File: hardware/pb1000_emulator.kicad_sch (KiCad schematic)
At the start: 1 part, among them U1 Raspberry Pi Pico 2 (RP2350)

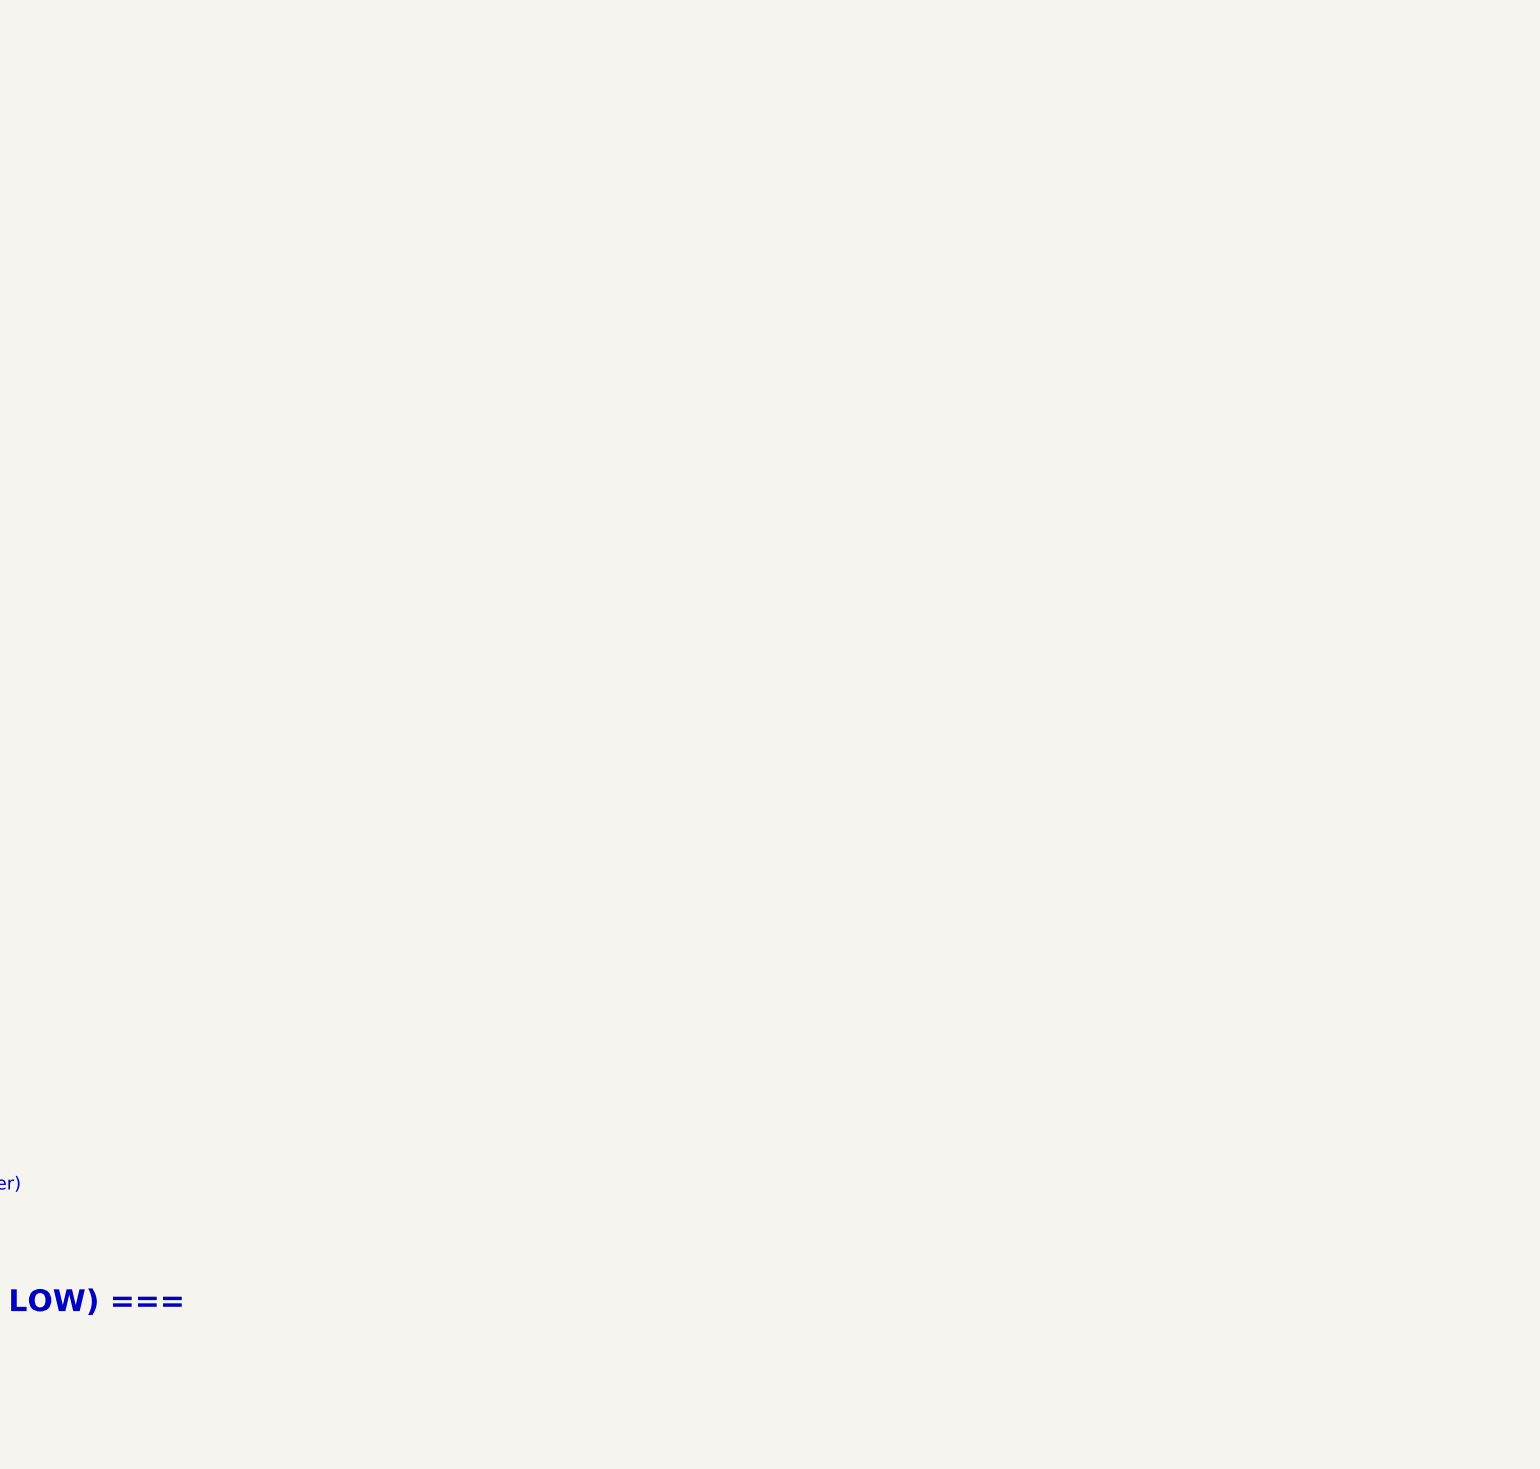
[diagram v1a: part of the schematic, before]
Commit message: VFDDがデバッグ動作のままで性能が低下していたのを修正、FDイメージ操作ツールでPCからのファイル転送時に必ずファイル名を大文字にするよう修正(Claude Code)
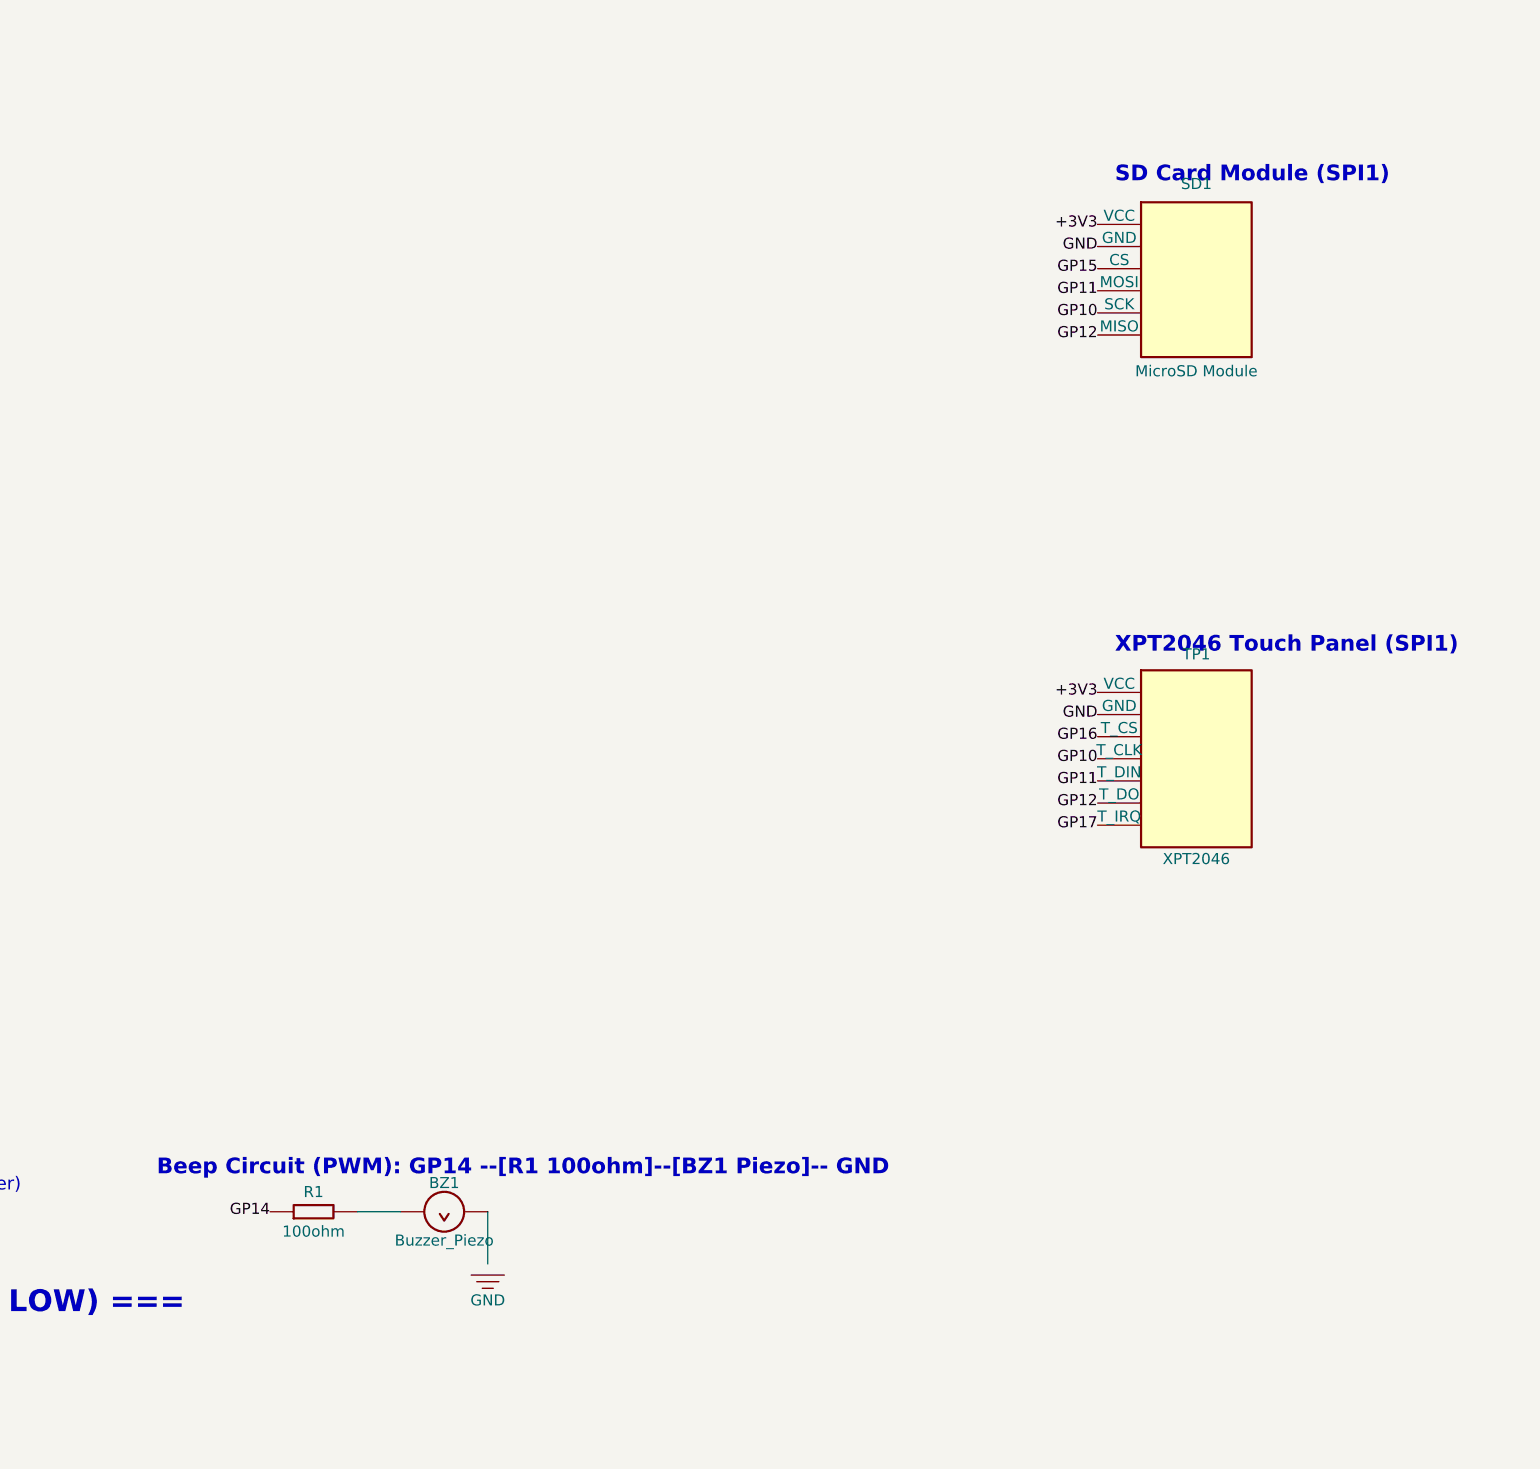
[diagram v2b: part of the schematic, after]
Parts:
- added BZ1: Buzzer_Piezo, symbol Local:Buzzer_Piezo
- added R1: 100ohm, symbol Local:R
- added SD1: MicroSD Module, symbol Local:SD_Card
- added TP1: XPT2046, symbol Local:XPT2046
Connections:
- new net: BZ1.1 (+), R1.2
- new net +3V3: SD1.1 (VCC), TP1.1 (VCC)
- new net GND: BZ1.2 (K), SD1.2 (GND), TP1.2 (GND)
- new net GP10: SD1.5 (SCK), TP1.4 (T_CLK)
- new net GP11: SD1.4 (MOSI), TP1.5 (T_DIN)
- new net GP12: SD1.6 (MISO), TP1.6 (T_DO)
- new net GP14: R1.1
- new net GP15: SD1.3 (CS)
- new net GP16: TP1.3 (T_CS)
- new net GP17: TP1.7 (T_IRQ)
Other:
- note added: "Beep Circuit (PWM): GP14 --[R1 100ohm]--[BZ1 Piezo]-- GND"
- note added: "SD Card Module (SPI1)"
- note added: "XPT2046 Touch Panel (SPI1)"
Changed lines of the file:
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@@
     (effects (font (size 1.5 1.5)) (justify left))
   )
+  (text "Beep Circuit (PWM): GP14 --[R1 100ohm]--[BZ1 Piezo]-- GND" (at 232 202 0)
+    (effects (font (size 1.8 1.8) (bold yes)) (justify left))
+  )
+  (label "GP14" (at 245 207 180)
+    (effects (font (size 1.27 1.27)) (justify right))
+  )
+  (symbol (lib_id "Local:R") (at 250 207 0) (unit 1)
+    (in_bom yes) (on_board yes) (fields_autoplaced)
+    (property "Reference" "R1" (id 0) (at 250 204.73 0)
+      (effects (font (size 1.27 1.27)))
+    )
+    (property "Value" "100ohm" (id 1) (at 250 209.27 0)
+      (effects (font (size 1.27 1.27)))
+    )
+  )
+  (wire (pts (xy 255 207) (xy 260 207))
+    (stroke (width 0) (type default))
+  )
+  (symbol (lib_id "Local:Buzzer_Piezo") (at 265 207 0) (unit 1)
+    (in_bom yes) (on_board yes) (fields_autoplaced)
+    (property "Reference" "BZ1" (id 0) (at 265 203.698 0)
+      (effects (font (size 1.27 1.27)))
+    )
+    (property "Value" "Buzzer_Piezo" (id 1) (at 265 210.302 0)
+      (effects (font (size 1.27 1.27)))
+    )
+  )
+  (wire (pts (xy 270 207) (xy 270 213))
+    (stroke (width 0) (type default))
+  )
+  (symbol (lib_id "power:GND") (at 270 213 0) (unit 1)
+    (in_bom yes) (on_board yes) (fields_autoplaced)
+    (property "Reference" "#PWR01" (id 0) (at 270 213 0)
+      (effects (font (size 1.27 1.27)) hide)
+    )
+    (property "Value" "GND" (id 1) (at 270 217.17 0)
+      (effects (font (size 1.27 1.27)))
+    )
+  )
+  (text "SD Card Module (SPI1)" (at 342 88 0)
+    (effects (font (size 1.8 1.8) (bold yes)) (justify left))
+  )
+  (symbol (lib_id "Local:SD_Card") (at 345 100 0) (unit 1)
+    (in_bom yes) (on_board yes) (fields_autoplaced)
+    (property "Reference" "SD1" (id 0) (at 351.35 89 0)
+      (effects (font (size 1.27 1.27)))
+    )
+    (property "Value" "MicroSD Module" (id 1) (at 351.35 110.5 0)
+      (effects (font (size 1.27 1.27)))
+    )
+  )
+  (label "+3V3" (at 340 93.65 180)
+    (effects (font (size 1.27 1.27)) (justify right))
+  )
+  (label "GND" (at 340 96.19 180)
+    (effects (font (size 1.27 1.27)) (justify right))
+  )
+  (label "GP15" (at 340 98.73 180)
+    (effects (font (size 1.27 1.27)) (justify right))
+  )
+  (label "GP11" (at 340 101.27 180)
+    (effects (font (size 1.27 1.27)) (justify right))
+  )
+  (label "GP10" (at 340 103.81 180)
+    (effects (font (size 1.27 1.27)) (justify right))
+  )
+  (label "GP12" (at 340 106.35 180)
+    (effects (font (size 1.27 1.27)) (justify right))
+  )
+  (text "XPT2046 Touch Panel (SPI1)" (at 342 142 0)
+    (effects (font (size 1.8 1.8) (bold yes)) (justify left))
+  )
+  (symbol (lib_id "Local:XPT2046") (at 345 155 0) (unit 1)
+    (in_bom yes) (on_board yes) (fields_autoplaced)
+    (property "Reference" "TP1" (id 0) (at 351.35 143 0)
+      (effects (font (size 1.27 1.27)))
+    )
+    (property "Value" "XPT2046" (id 1) (at 351.35 166.5 0)
+      (effects (font (size 1.27 1.27)))
+    )
+  )
+  (label "+3V3" (at 340 147.38 180)
+    (effects (font (size 1.27 1.27)) (justify right))
+  )
+  (label "GND" (at 340 149.92 180)
+    (effects (font (size 1.27 1.27)) (justify right))
+  )
+  (label "GP16" (at 340 152.46 180)
+    (effects (font (size 1.27 1.27)) (justify right))
+  )
+  (label "GP10" (at 340 155 180)
+    (effects (font (size 1.27 1.27)) (justify right))
+  )
+  (label "GP11" (at 340 157.54 180)
+    (effects (font (size 1.27 1.27)) (justify right))
+  )
+  (label "GP12" (at 340 160.08 180)
+    (effects (font (size 1.27 1.27)) (justify right))
+  )
+  (label "GP17" (at 340 162.62 180)
+    (effects (font (size 1.27 1.27)) (justify right))
+  )
 )

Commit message: タイマー機能の実装ほぼ完了(Claude Code)
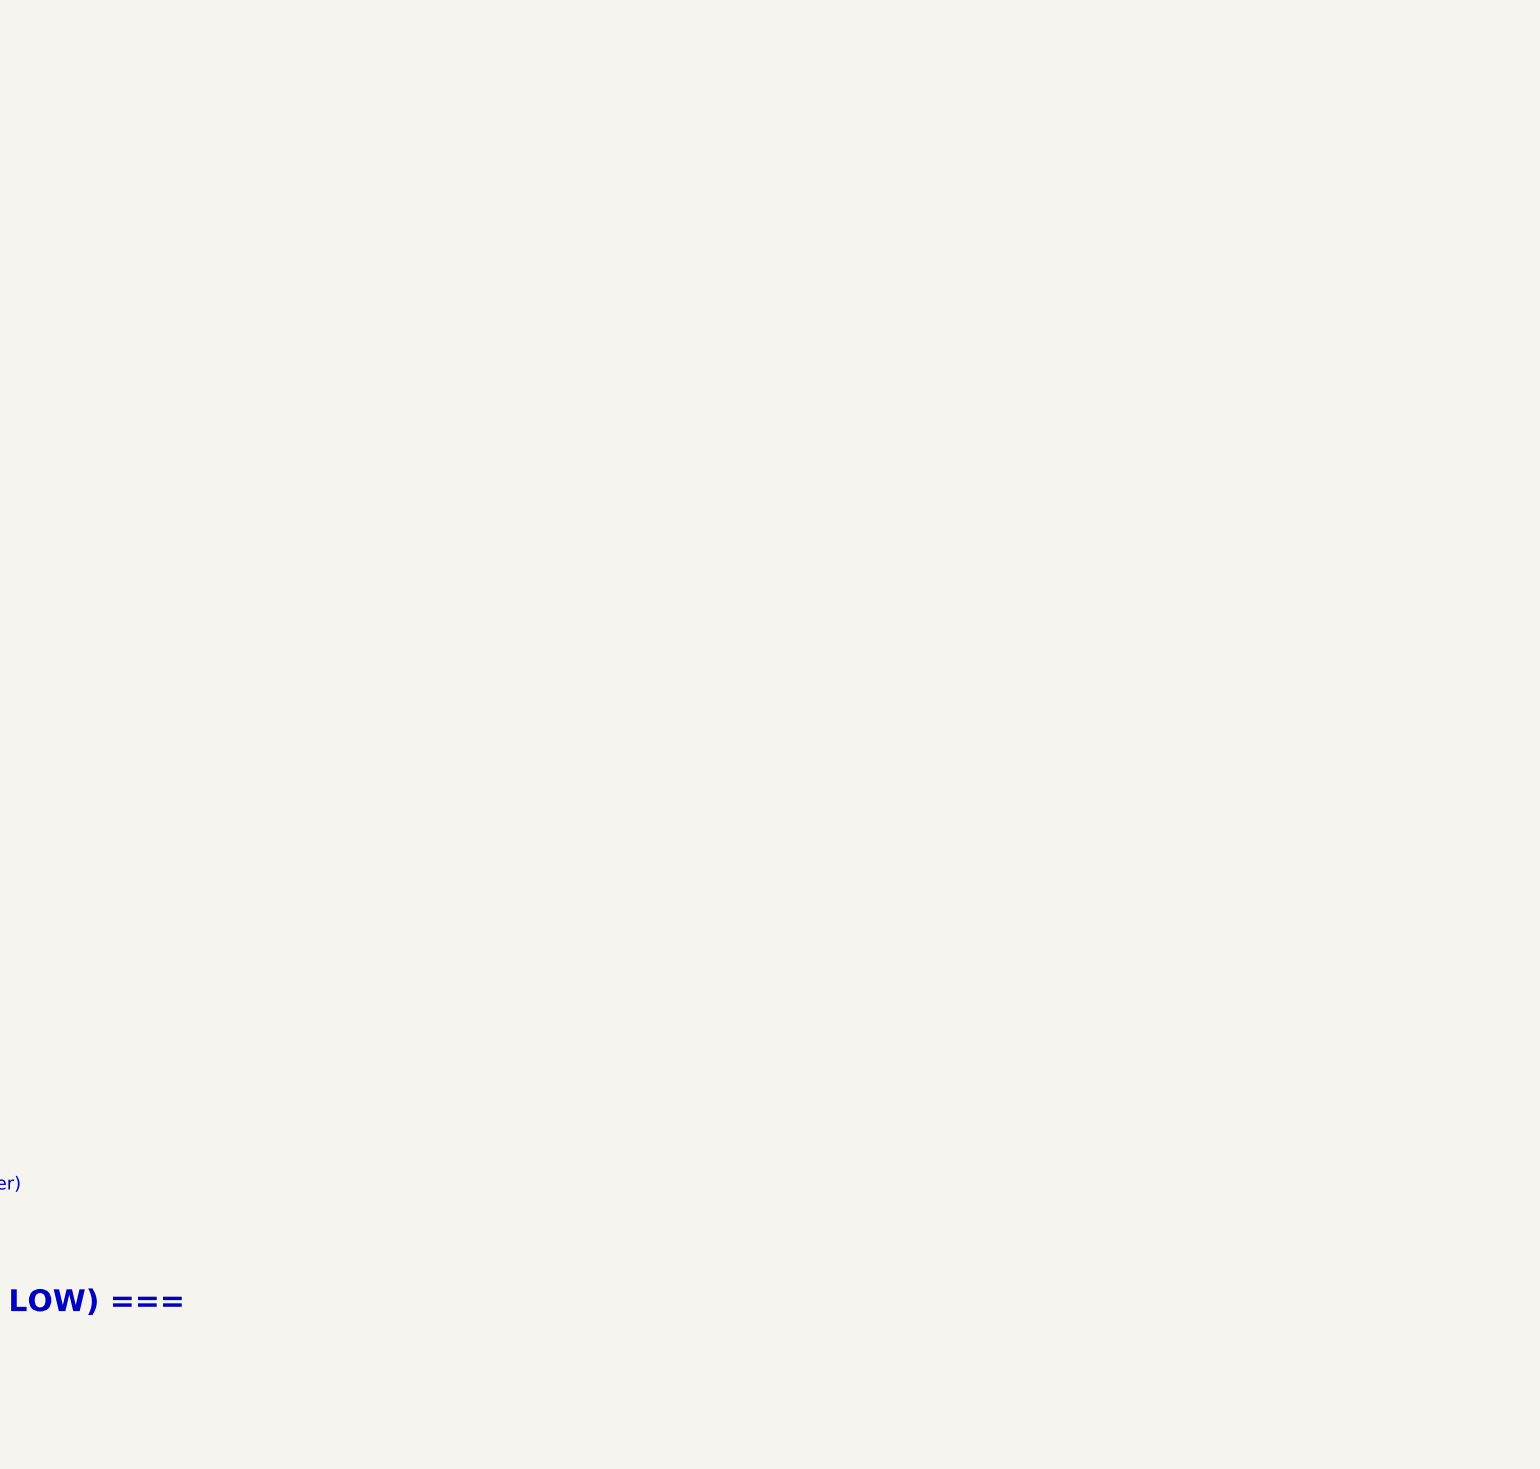
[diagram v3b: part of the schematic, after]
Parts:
- removed BZ1: Buzzer_Piezo, symbol Local:Buzzer_Piezo
- removed R1: 100ohm, symbol Local:R
- removed SD1: MicroSD Module, symbol Local:SD_Card
- removed TP1: XPT2046, symbol Local:XPT2046
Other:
- note removed: "Beep Circuit (PWM): GP14 --[R1 100ohm]--[BZ1 Piezo]-- GND"
- note removed: "SD Card Module (SPI1)"
- note removed: "XPT2046 Touch Panel (SPI1)"
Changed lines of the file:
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@@
     (effects (font (size 1.5 1.5)) (justify left))
   )
-  (text "Beep Circuit (PWM): GP14 --[R1 100ohm]--[BZ1 Piezo]-- GND" (at 232 202 0)
-    (effects (font (size 1.8 1.8) (bold yes)) (justify left))
-  )
-  (label "GP14" (at 245 207 180)
-    (effects (font (size 1.27 1.27)) (justify right))
-  )
-  (symbol (lib_id "Local:R") (at 250 207 0) (unit 1)
-    (in_bom yes) (on_board yes) (fields_autoplaced)
-    (property "Reference" "R1" (id 0) (at 250 204.73 0)
-      (effects (font (size 1.27 1.27)))
-    )
-    (property "Value" "100ohm" (id 1) (at 250 209.27 0)
-      (effects (font (size 1.27 1.27)))
-    )
-  )
-  (wire (pts (xy 255 207) (xy 260 207))
-    (stroke (width 0) (type default))
-  )
-  (symbol (lib_id "Local:Buzzer_Piezo") (at 265 207 0) (unit 1)
-    (in_bom yes) (on_board yes) (fields_autoplaced)
-    (property "Reference" "BZ1" (id 0) (at 265 203.698 0)
-      (effects (font (size 1.27 1.27)))
-    )
-    (property "Value" "Buzzer_Piezo" (id 1) (at 265 210.302 0)
-      (effects (font (size 1.27 1.27)))
-    )
-  )
-  (wire (pts (xy 270 207) (xy 270 213))
-    (stroke (width 0) (type default))
-  )
-  (symbol (lib_id "power:GND") (at 270 213 0) (unit 1)
-    (in_bom yes) (on_board yes) (fields_autoplaced)
-    (property "Reference" "#PWR01" (id 0) (at 270 213 0)
-      (effects (font (size 1.27 1.27)) hide)
-    )
-    (property "Value" "GND" (id 1) (at 270 217.17 0)
-      (effects (font (size 1.27 1.27)))
-    )
-  )
-  (text "SD Card Module (SPI1)" (at 342 88 0)
-    (effects (font (size 1.8 1.8) (bold yes)) (justify left))
-  )
-  (symbol (lib_id "Local:SD_Card") (at 345 100 0) (unit 1)
-    (in_bom yes) (on_board yes) (fields_autoplaced)
-    (property "Reference" "SD1" (id 0) (at 351.35 89 0)
-      (effects (font (size 1.27 1.27)))
-    )
-    (property "Value" "MicroSD Module" (id 1) (at 351.35 110.5 0)
-      (effects (font (size 1.27 1.27)))
-    )
-  )
-  (label "+3V3" (at 340 93.65 180)
-    (effects (font (size 1.27 1.27)) (justify right))
-  )
-  (label "GND" (at 340 96.19 180)
-    (effects (font (size 1.27 1.27)) (justify right))
-  )
-  (label "GP15" (at 340 98.73 180)
-    (effects (font (size 1.27 1.27)) (justify right))
-  )
-  (label "GP11" (at 340 101.27 180)
-    (effects (font (size 1.27 1.27)) (justify right))
-  )
-  (label "GP10" (at 340 103.81 180)
-    (effects (font (size 1.27 1.27)) (justify right))
-  )
-  (label "GP12" (at 340 106.35 180)
-    (effects (font (size 1.27 1.27)) (justify right))
-  )
-  (text "XPT2046 Touch Panel (SPI1)" (at 342 142 0)
-    (effects (font (size 1.8 1.8) (bold yes)) (justify left))
-  )
-  (symbol (lib_id "Local:XPT2046") (at 345 155 0) (unit 1)
-    (in_bom yes) (on_board yes) (fields_autoplaced)
-    (property "Reference" "TP1" (id 0) (at 351.35 143 0)
-      (effects (font (size 1.27 1.27)))
-    )
-    (property "Value" "XPT2046" (id 1) (at 351.35 166.5 0)
-      (effects (font (size 1.27 1.27)))
-    )
-  )
-  (label "+3V3" (at 340 147.38 180)
-    (effects (font (size 1.27 1.27)) (justify right))
-  )
-  (label "GND" (at 340 149.92 180)
-    (effects (font (size 1.27 1.27)) (justify right))
-  )
-  (label "GP16" (at 340 152.46 180)
-    (effects (font (size 1.27 1.27)) (justify right))
-  )
-  (label "GP10" (at 340 155 180)
-    (effects (font (size 1.27 1.27)) (justify right))
-  )
-  (label "GP11" (at 340 157.54 180)
-    (effects (font (size 1.27 1.27)) (justify right))
-  )
-  (label "GP12" (at 340 160.08 180)
-    (effects (font (size 1.27 1.27)) (justify right))
-  )
-  (label "GP17" (at 340 162.62 180)
-    (effects (font (size 1.27 1.27)) (justify right))
-  )
 )
